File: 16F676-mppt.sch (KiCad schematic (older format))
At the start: 49 parts, among them J1 S+, J2 S-, J3 VB+, J4 VB-, Q1 BUK9511-55A127, Q2 BUK9511-55A127, Q3 2N2222A, Q4 2N2222A, Q5 2N2907A, SW1 Write OP-AMP DIFF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

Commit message: change op-amp multiplier resisters.
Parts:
- R1: value 4.7k -> 10k
- R15: value 10k -> 47k
- R2, R4: value 300k -> 100k
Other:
- note added: "x47(50, 6A)"
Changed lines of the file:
@@
 Sheet 1 1
 Title "Simple MPPT with 16F676 v1"
-Date "2018-06-12"
-Rev "1.1"
+Date "2018-07-04"
+Rev "1.2"
 Comp ""
 Comment1 ""
@@
 P 7300 4250
 F 0 "R4" V 7380 4250 50  0000 C CNN
-F 1 "300k" V 7300 4250 50  0000 C CNN
+F 1 "100k" V 7300 4250 50  0000 C CNN
 F 2 "Resistors_THT:R_Axial_DIN0309_L9.0mm_D3.2mm_P12.70mm_Horizontal" V 7230 4250 30  0001 C CNN
 F 3 "" H 7300 4250 30  0000 C CNN
@@
 P 6950 5300
 F 0 "R2" V 7030 5300 50  0000 C CNN
-F 1 "300k" V 6950 5300 50  0000 C CNN
+F 1 "100k" V 6950 5300 50  0000 C CNN
 F 2 "Resistors_THT:R_Axial_DIN0309_L9.0mm_D3.2mm_P12.70mm_Horizontal" V 6880 5300 30  0001 C CNN
 F 3 "" H 6950 5300 30  0000 C CNN
@@
 P 9450 4850
 F 0 "R1" V 9530 4850 50  0000 C CNN
-F 1 "4.7k" V 9450 4850 50  0000 C CNN
+F 1 "10k" V 9450 4850 50  0000 C CNN
 F 2 "Resistors_THT:R_Axial_DIN0309_L9.0mm_D3.2mm_P12.70mm_Horizontal" V 9380 4850 50  0001 C CNN
 F 3 "" H 9450 4850 50  0000 C CNN
@@
 P 9900 4300
 F 0 "R15" V 9980 4300 50  0000 C CNN
-F 1 "10k" V 9900 4300 50  0000 C CNN
+F 1 "47k" V 9900 4300 50  0000 C CNN
 F 2 "Resistors_THT:R_Axial_DIN0309_L9.0mm_D3.2mm_P12.70mm_Horizontal" V 9830 4300 50  0001 C CNN
 F 3 "" H 9900 4300 50  0000 C CNN
@@
 Connection ~ 8250 4850
 Connection ~ 9200 4850
+Text Notes 9100 3850 0    60   ~ 0
+x47(50, 6A)
 $EndSCHEMATC

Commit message: update op-amp resister.
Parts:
- R1: value 10k -> 2.2k
- R15: value 47k -> 10k
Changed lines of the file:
@@
 P 9450 4850
 F 0 "R1" V 9530 4850 50  0000 C CNN
-F 1 "10k" V 9450 4850 50  0000 C CNN
+F 1 "2.2k" V 9450 4850 50  0000 C CNN
 F 2 "Resistors_THT:R_Axial_DIN0309_L9.0mm_D3.2mm_P12.70mm_Horizontal" V 9380 4850 50  0001 C CNN
 F 3 "" H 9450 4850 50  0000 C CNN
@@
 P 9900 4300
 F 0 "R15" V 9980 4300 50  0000 C CNN
-F 1 "47k" V 9900 4300 50  0000 C CNN
+F 1 "10k" V 9900 4300 50  0000 C CNN
 F 2 "Resistors_THT:R_Axial_DIN0309_L9.0mm_D3.2mm_P12.70mm_Horizontal" V 9830 4300 50  0001 C CNN
 F 3 "" H 9900 4300 50  0000 C CNN

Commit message: minor changes.
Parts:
- C1, C2, C3, C5, C6, C7: symbol CP -> Device:CP
- C4: symbol C -> Device:C
- D1, D10, D11, D2, D6, D7: symbol D_Schottky -> Device:D_Schottky
- D3, D5: symbol D -> Device:D
- D4, D8, D9: symbol LED-RESCUE-12f675-mppt -> 16F676-mppt-rescue:LED-RESCUE-12f675-mppt
- J1, J2, J3, J4: symbol Conn_01x01 -> 16F676-mppt-rescue:Conn_01x01
- L1, L2: symbol INDUCTOR -> 16F676-mppt-rescue:INDUCTOR
- Q1, Q2: symbol Q_NMOS_GDS -> Device:Q_NMOS_GDS
- Q3, Q4: symbol Q_NPN_EBC -> Device:Q_NPN_EBC
- Q5: symbol Q_PNP_EBC -> Device:Q_PNP_EBC
- R1, R10, R11, R12, R13, R14, R15, R16, R2, R3, R4, R5, R6, R7, R8, R9: symbol R -> Device:R
- SW1: symbol SW_PUSH -> 16F676-mppt-rescue:SW_PUSH
- U1: symbol LM7805_TO220 -> 16F676-mppt-rescue:LM7805_TO220
- U2: symbol LM358N-RESCUE-12f675-mppt -> 16F676-mppt-rescue:LM358N-RESCUE-12f675-mppt
- U3: symbol 16F676 -> 16F676-mppt-rescue:16F676
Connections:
- wire segments 136 -> 191

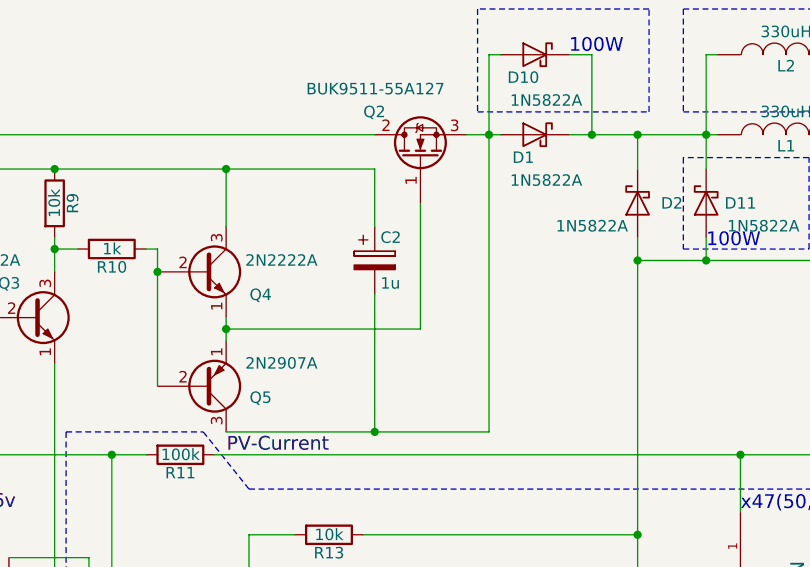
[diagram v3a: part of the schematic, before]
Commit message: Fix FET Bootstrap capacitor.
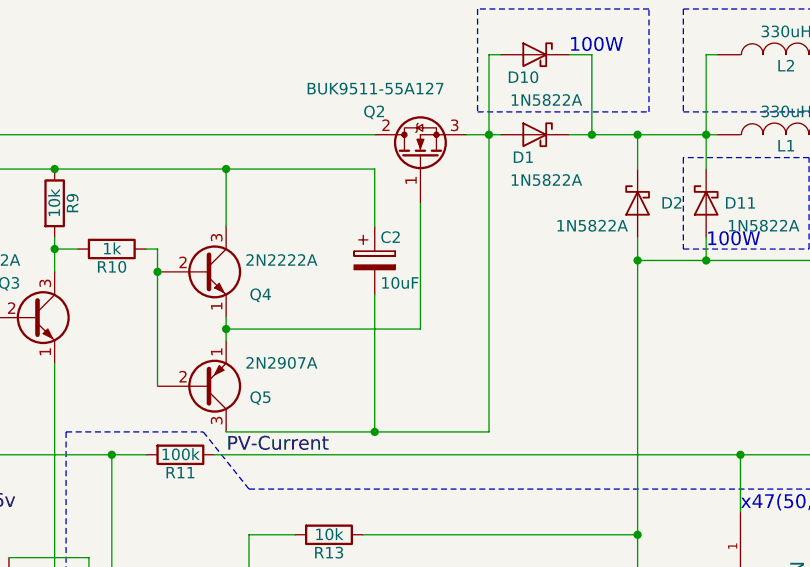
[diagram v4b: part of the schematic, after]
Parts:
- C2: value 1u -> 10uF
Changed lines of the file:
@@
 P 7500 2750
 F 0 "C2" H 7525 2850 50  0000 L CNN
-F 1 "1u" H 7525 2650 50  0000 L CNN
+F 1 "10uF" H 7525 2650 50  0000 L CNN
 F 2 "Capacitors_THT:CP_Radial_D12.5mm_P5.00mm" H 7538 2600 30  0001 C CNN
 F 3 "" H 7500 2750 60  0000 C CNN

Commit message: Bootstrap capacitor to 47uF.
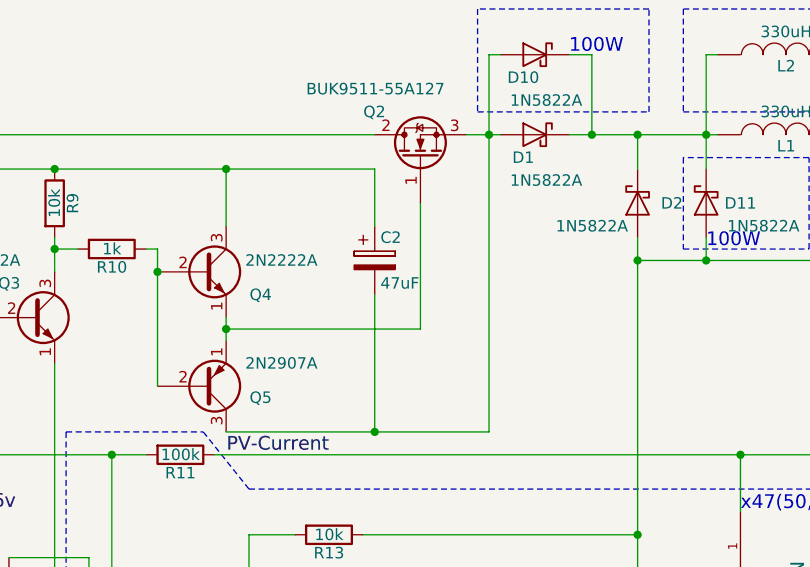
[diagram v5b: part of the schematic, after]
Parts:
- C2: value 10uF -> 47uF
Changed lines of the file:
@@
 Sheet 1 1
 Title "Simple MPPT with 16F676 v1"
-Date "2018-07-04"
-Rev "1.2"
+Date "2018-11-15"
+Rev "1.3"
 Comp ""
 Comment1 ""
@@
 P 7500 2750
 F 0 "C2" H 7525 2850 50  0000 L CNN
-F 1 "10uF" H 7525 2650 50  0000 L CNN
+F 1 "47uF" H 7525 2650 50  0000 L CNN
 F 2 "Capacitors_THT:CP_Radial_D12.5mm_P5.00mm" H 7538 2600 30  0001 C CNN
 F 3 "" H 7500 2750 60  0000 C CNN

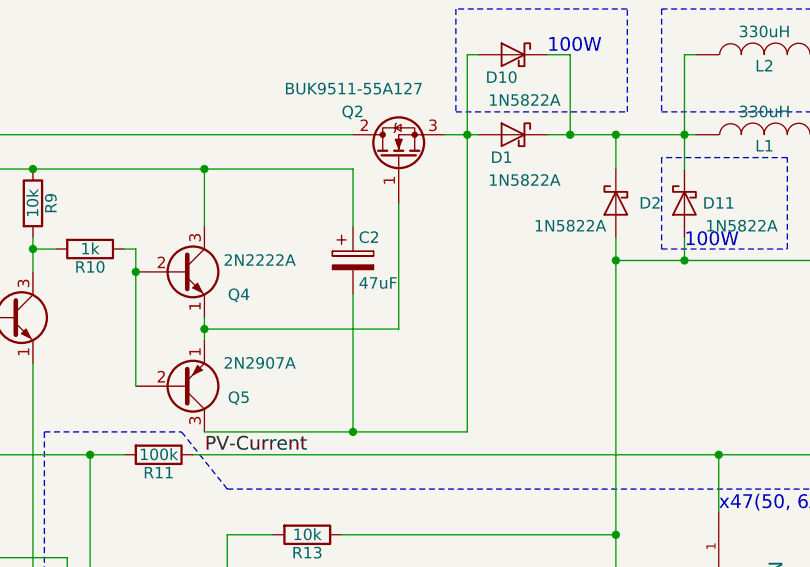
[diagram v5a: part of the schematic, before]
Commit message: Revert Bootstrap capacitor to 10uF.
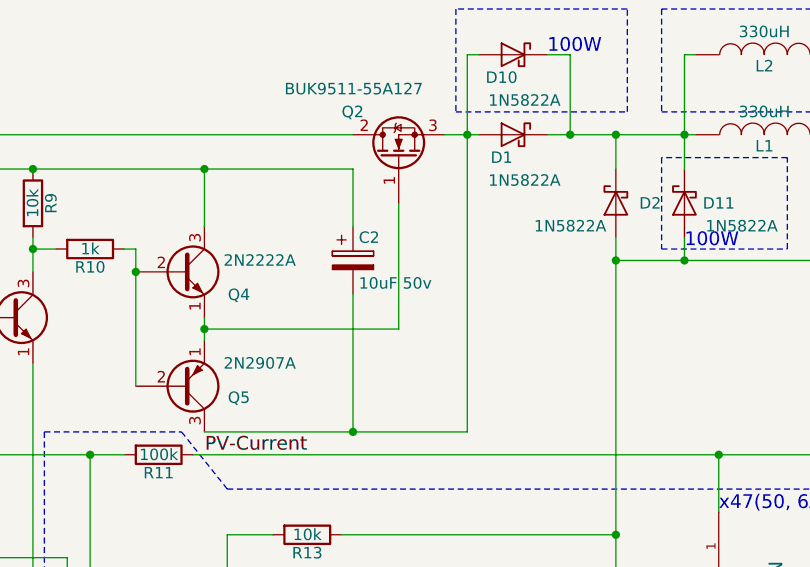
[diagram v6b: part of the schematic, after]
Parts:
- C2: value 47uF -> 10uF 50v
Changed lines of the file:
@@
 P 7500 2750
 F 0 "C2" H 7525 2850 50  0000 L CNN
-F 1 "47uF" H 7525 2650 50  0000 L CNN
+F 1 "10uF 50v" H 7525 2650 50  0000 L CNN
 F 2 "Capacitors_THT:CP_Radial_D12.5mm_P5.00mm" H 7538 2600 30  0001 C CNN
 F 3 "" H 7500 2750 60  0000 C CNN

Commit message: Add resistor
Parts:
- added R17: 1k, Resistors_THT:R_Axial_DIN0309_L9.0mm_D3.2mm_P12.70mm_Horizontal, symbol Device:R
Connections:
- net at Q4.1 (E), Q5.1 (E): now also R17.1; no longer Q2.1 (G)
- new net: Q2.1 (G), R17.2
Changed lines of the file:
@@
 	7900 2200 8000 2200
-Wire Wire Line
-	6850 3000 6850 3050
-Wire Wire Line
-	6850 3050 7700 3050
-Wire Wire Line
-	7700 3050 7700 2500
-Connection ~ 6850 3050
 Wire Wire Line
 	8000 3500 7500 3500
@@
 	8650 2200 8950 2200
 Wire Wire Line
+	8000 2200 8050 2200
+Wire Wire Line
+	7500 3500 6850 3500
+Wire Wire Line
+	6100 5600 5900 5600
+Wire Wire Line
+	6100 2350 6850 2350
+Wire Wire Line
+	6550 2800 6550 3300
+Wire Wire Line
+	6100 2700 6100 2800
+Wire Wire Line
+	1900 2200 2400 2200
+Wire Wire Line
+	2300 5600 1500 5600
+Wire Wire Line
+	1500 2200 1900 2200
+Wire Wire Line
+	1500 3500 1500 3900
+Wire Wire Line
+	4100 5600 2300 5600
+Wire Wire Line
+	2750 4100 3400 4100
+Wire Wire Line
+	2750 3400 3150 3400
+Wire Wire Line
+	3400 4100 4500 4100
+Wire Wire Line
+	3400 3400 3500 3400
+Wire Wire Line
+	6850 2350 7500 2350
+Wire Wire Line
+	7650 5600 7150 5600
+Wire Wire Line
+	7650 4450 8400 4450
+Wire Wire Line
+	8650 2750 8650 3950
+Wire Wire Line
+	9750 2750 10500 2750
+Wire Wire Line
+	9750 2200 10500 2200
+Wire Wire Line
+	1500 5600 1250 5600
+Wire Wire Line
+	6950 5600 6350 5600
+Wire Wire Line
+	6950 4750 6950 5150
+Wire Wire Line
+	8650 3950 8650 5200
+Wire Wire Line
+	5900 5600 5450 5600
+Wire Wire Line
+	6350 5600 6100 5600
+Wire Wire Line
+	6350 3600 6500 3600
+Wire Wire Line
+	5450 5600 4100 5600
+Wire Wire Line
+	5450 4400 5650 4400
+Wire Wire Line
+	5900 4500 5900 4650
+Wire Wire Line
+	5750 4500 5750 6000
+Wire Wire Line
+	8650 5600 7650 5600
+Wire Wire Line
+	9700 4850 9700 5600
+Wire Wire Line
+	8400 4450 8700 4450
+Wire Wire Line
+	9100 3600 9900 3600
+Wire Wire Line
+	2950 2200 7500 2200
+Wire Wire Line
+	2950 2200 2950 2600
+Wire Wire Line
+	3150 5000 3150 6100
+Wire Wire Line
+	3800 4650 3800 5000
+Wire Wire Line
+	2300 4650 2300 5600
+Wire Wire Line
+	2400 2200 2600 2200
+Wire Wire Line
+	8450 2200 8650 2200
+Wire Wire Line
+	8950 2750 9750 2750
+Wire Wire Line
+	8950 2200 8950 2350
+Wire Wire Line
+	8950 2200 9000 2200
+$Comp
+L Device:R R17
+U 1 1 5BF07E56
+P 7200 3050
+F 0 "R17" V 7280 3050 50  0000 C CNN
+F 1 "1k" V 7200 3050 50  0000 C CNN
+F 2 "Resistors_THT:R_Axial_DIN0309_L9.0mm_D3.2mm_P12.70mm_Horizontal" V 7130 3050 30  0001 C CNN
+F 3 "" H 7200 3050 30  0000 C CNN
+	1    7200 3050
+	0    -1   -1   0
+$EndComp
+Wire Wire Line
+	6850 3000 6850 3050
+Wire Wire Line
+	7050 3050 6850 3050
+Wire Wire Line
+	8000 2200 8000 3500
+Connection ~ 6850 3050
+Wire Wire Line
 	6850 3050 6850 3100
 Wire Wire Line
-	8000 2200 8050 2200
-Wire Wire Line
-	8000 2200 8000 3500
-Wire Wire Line
-	7500 3500 6850 3500
-Wire Wire Line
-	6100 5600 5900 5600
-Wire Wire Line
-	6100 2350 6850 2350
-Wire Wire Line
-	6550 2800 6550 3300
-Wire Wire Line
-	6100 2700 6100 2800
-Wire Wire Line
-	1900 2200 2400 2200
-Wire Wire Line
-	2300 5600 1500 5600
-Wire Wire Line
-	1500 2200 1900 2200
-Wire Wire Line
-	1500 3500 1500 3900
-Wire Wire Line
-	4100 5600 2300 5600
-Wire Wire Line
-	2750 4100 3400 4100
-Wire Wire Line
-	2750 3400 3150 3400
-Wire Wire Line
-	3400 4100 4500 4100
-Wire Wire Line
-	3400 3400 3500 3400
-Wire Wire Line
-	6850 2350 7500 2350
-Wire Wire Line
-	7650 5600 7150 5600
-Wire Wire Line
-	7650 4450 8400 4450
-Wire Wire Line
-	8650 2750 8650 3950
-Wire Wire Line
-	9750 2750 10500 2750
-Wire Wire Line
-	9750 2200 10500 2200
-Wire Wire Line
-	1500 5600 1250 5600
-Wire Wire Line
-	6950 5600 6350 5600
-Wire Wire Line
-	6950 4750 6950 5150
-Wire Wire Line
-	8650 3950 8650 5200
-Wire Wire Line
-	5900 5600 5450 5600
-Wire Wire Line
-	6350 5600 6100 5600
-Wire Wire Line
-	6350 3600 6500 3600
-Wire Wire Line
-	5450 5600 4100 5600
-Wire Wire Line
-	5450 4400 5650 4400
-Wire Wire Line
-	5900 4500 5900 4650
-Wire Wire Line
-	5750 4500 5750 6000
-Wire Wire Line
-	8650 5600 7650 5600
-Wire Wire Line
-	9700 4850 9700 5600
-Wire Wire Line
-	8400 4450 8700 4450
-Wire Wire Line
-	9100 3600 9900 3600
-Wire Wire Line
-	2950 2200 7500 2200
-Wire Wire Line
-	2950 2200 2950 2600
-Wire Wire Line
-	3150 5000 3150 6100
-Wire Wire Line
-	3800 4650 3800 5000
-Wire Wire Line
-	2300 4650 2300 5600
-Wire Wire Line
-	2400 2200 2600 2200
-Wire Wire Line
-	8450 2200 8650 2200
-Wire Wire Line
-	8950 2750 9750 2750
-Wire Wire Line
-	8950 2200 8950 2350
-Wire Wire Line
-	8950 2200 9000 2200
+	7350 3050 7700 3050
+Wire Wire Line
+	7700 3050 7700 2500
 $EndSCHEMATC

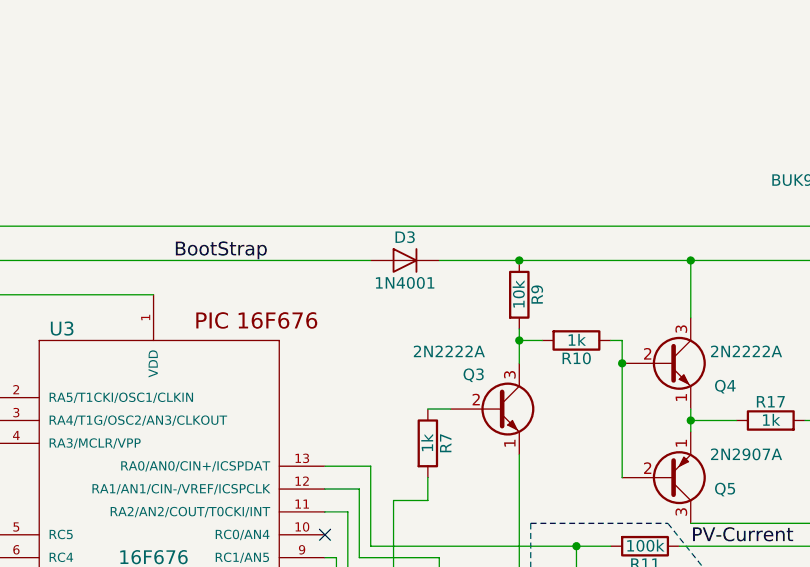
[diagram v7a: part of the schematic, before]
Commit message: change bootstrap diode
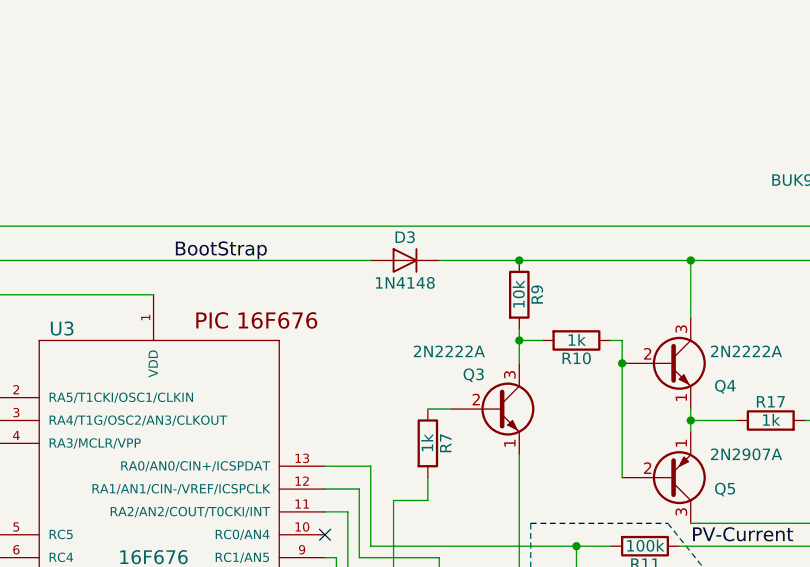
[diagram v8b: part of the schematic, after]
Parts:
- D3: value 1N4001 -> 1N4148
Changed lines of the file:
@@
 P 5600 2350
 F 0 "D3" H 5600 2450 50  0000 C CNN
-F 1 "1N4001" H 5600 2250 50  0000 C CNN
+F 1 "1N4148" H 5600 2250 50  0000 C CNN
 F 2 "Diodes_THT:D_DO-41_SOD81_P10.16mm_Horizontal" H 5600 2350 60  0001 C CNN
 F 3 "" H 5600 2350 60  0000 C CNN
